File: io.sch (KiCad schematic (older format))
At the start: 13 parts, among them J5 USB_C_Receptacle_USB2.0, J6 Conn_ARM_JTAG_SWD_10, J7 UART, J8 Conn_02x14_Odd_Even

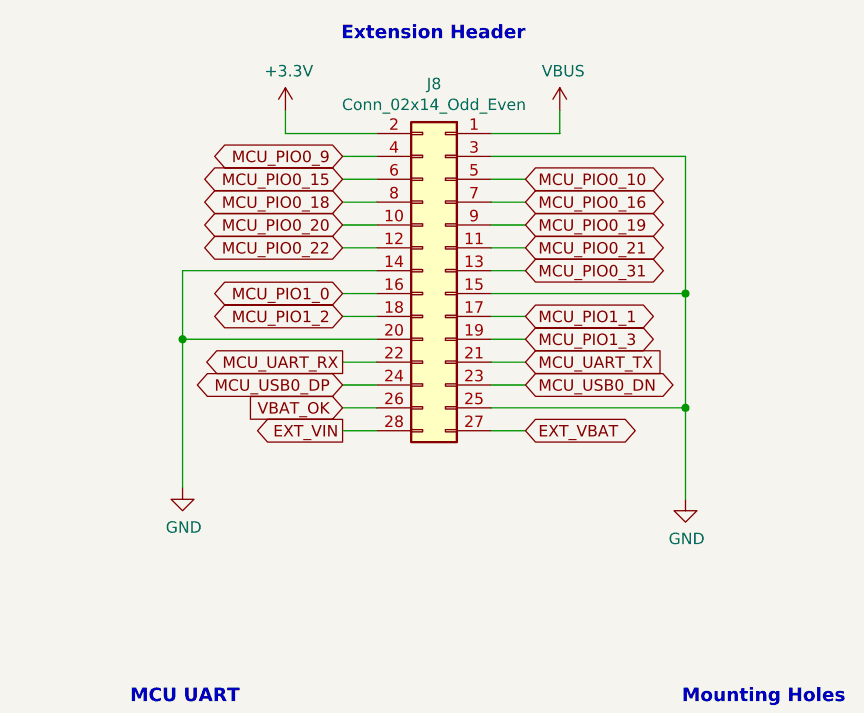
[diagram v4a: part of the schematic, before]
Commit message: Changed pin assignment on mcu and extension header
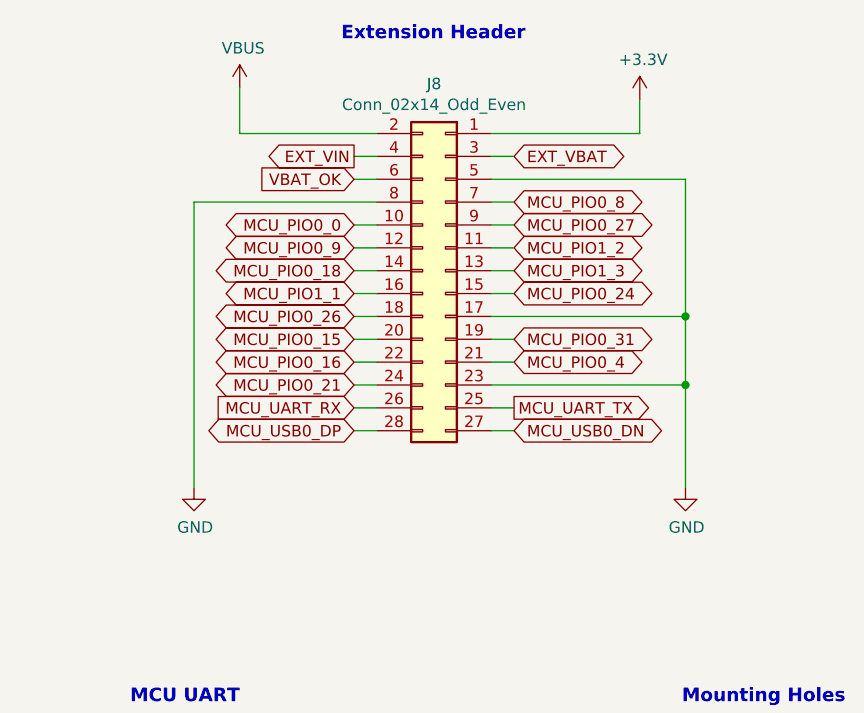
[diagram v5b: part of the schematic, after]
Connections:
- net MCU_PIO0_10 is gone; now on net GND: J8.5 (Pin_5)
- net MCU_PIO0_22 is gone; now on net MCU_PIO0_9: J8.12 (Pin_12)
- net MCU_PIO1_0 is gone; now on net MCU_PIO1_1: J8.16 (Pin_16)
- net +3V3: now also J8.1 (Pin_1); no longer J8.2 (Pin_2)
- net EXT_VBAT: now also J8.3 (Pin_3); no longer J8.27 (Pin_27)
- net EXT_VIN: now also J8.4 (Pin_4); no longer J8.28 (Pin_28)
- net GND: now also J8.17 (Pin_17), J8.23 (Pin_23), J8.8 (Pin_8); no longer J8.14 (Pin_14), J8.15 (Pin_15), J8.20 (Pin_20), J8.25 (Pin_25), J8.3 (Pin_3)
- net MCU_PIO0_15: now also J8.20 (Pin_20); no longer J8.6 (Pin_6)
- net MCU_PIO0_16: now also J8.22 (Pin_22); no longer J8.7 (Pin_7)
- net MCU_PIO0_18: now also J8.14 (Pin_14); no longer J8.8 (Pin_8)
- net MCU_PIO0_21: now also J8.24 (Pin_24); no longer J8.11 (Pin_11)
- net MCU_PIO0_31: now also J8.19 (Pin_19); no longer J8.13 (Pin_13)
- net MCU_PIO0_9: no longer J8.4 (Pin_4)
- net MCU_PIO1_1: no longer J8.17 (Pin_17)
- net MCU_PIO1_2: now also J8.11 (Pin_11); no longer J8.18 (Pin_18)
- net MCU_PIO1_3: now also J8.13 (Pin_13); no longer J8.19 (Pin_19)
- net MCU_UART_RX: now also J8.26 (Pin_26); no longer J8.22 (Pin_22)
- net MCU_UART_TX: now also J8.25 (Pin_25); no longer J8.21 (Pin_21)
- net MCU_USB0_DN: now also J8.27 (Pin_27); no longer J8.23 (Pin_23)
- net MCU_USB0_DP: now also J8.28 (Pin_28); no longer J8.24 (Pin_24)
- net VBAT_OK: now also J8.6 (Pin_6); no longer J8.26 (Pin_26)
- net VBUS: now also J8.2 (Pin_2); no longer J8.1 (Pin_1)
- net MCU_PIO0_19 renamed MCU_PIO0_27
- net MCU_PIO0_20 renamed MCU_PIO0_0
- new net MCU_PIO0_24: J8.15 (Pin_15)
- new net MCU_PIO0_26: J8.18 (Pin_18)
- new net MCU_PIO0_4: J8.21 (Pin_21)
- new net MCU_PIO0_8: J8.7 (Pin_7)
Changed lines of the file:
@@
 	-1   0    0    -1
 $EndComp
-Text GLabel 7650 1700 0    50   BiDi ~ 0
+Text GLabel 8400 1700 2    50   BiDi ~ 0
+EXT_VBAT
+Text GLabel 7700 1700 0    50   Output ~ 0
+EXT_VIN
+Text GLabel 7700 1800 0    50   Input ~ 0
+VBAT_OK
+$Comp
+L power:VBUS #PWR0110
+U 1 1 5FB21530
+P 7200 1400
+F 0 "#PWR0110" H 7200 1250 50  0001 C CNN
+F 1 "VBUS" H 7215 1573 50  0000 C CNN
+F 2 "" H 7200 1400 50  0001 C CNN
+F 3 "" H 7200 1400 50  0001 C CNN
+	1    7200 1400
+	1    0    0    -1
+$EndComp
+Wire Wire Line
+	7200 1400 7200 1600
+Wire Wire Line
+	7200 1600 7800 1600
+$Comp
+L power:+3.3V #PWR0111
+U 1 1 5FB24107
+P 8950 1450
+F 0 "#PWR0111" H 8950 1300 50  0001 C CNN
+F 1 "+3.3V" H 8965 1623 50  0000 C CNN
+F 2 "" H 8950 1450 50  0001 C CNN
+F 3 "" H 8950 1450 50  0001 C CNN
+	1    8950 1450
+	1    0    0    -1
+$EndComp
+Wire Wire Line
+	8300 1600 8950 1600
+Wire Wire Line
+	8950 1600 8950 1450
+Text GLabel 8400 2900 2    50   BiDi ~ 0
+MCU_USB0_DN
+Text GLabel 7700 2900 0    50   BiDi ~ 0
+MCU_USB0_DP
+Text GLabel 8400 2800 2    50   Output ~ 0
+MCU_UART_TX
+Text GLabel 7700 2800 0    50   Input ~ 0
+MCU_UART_RX
+Text GLabel 8400 2600 2    50   BiDi ~ 0
+MCU_PIO0_4
+Text GLabel 7700 2700 0    50   BiDi ~ 0
+MCU_PIO0_21
+Text GLabel 7700 2600 0    50   BiDi ~ 0
+MCU_PIO0_16
+Text GLabel 7700 2500 0    50   BiDi ~ 0
+MCU_PIO0_15
+Text GLabel 8400 2500 2    50   BiDi ~ 0
+MCU_PIO0_31
+Text GLabel 8400 2300 2    50   BiDi ~ 0
+MCU_PIO0_24
+Text GLabel 8400 2200 2    50   BiDi ~ 0
+MCU_PIO1_3
+Text GLabel 8400 2100 2    50   BiDi ~ 0
+MCU_PIO1_2
+Text GLabel 7700 2400 0    50   BiDi ~ 0
+MCU_PIO0_26
+Text GLabel 7700 2300 0    50   BiDi ~ 0
+MCU_PIO1_1
+Text GLabel 7700 2200 0    50   BiDi ~ 0
+MCU_PIO0_18
+Text GLabel 7700 2100 0    50   BiDi ~ 0
 MCU_PIO0_9
-Text GLabel 8450 1800 2    50   BiDi ~ 0
-MCU_PIO0_10
-Text GLabel 7650 1800 0    50   BiDi ~ 0
-MCU_PIO0_15
-Text GLabel 7650 1900 0    50   BiDi ~ 0
-MCU_PIO0_18
-Text GLabel 7650 2000 0    50   BiDi ~ 0
-MCU_PIO0_20
-Text GLabel 7650 2100 0    50   BiDi ~ 0
-MCU_PIO0_22
-Text GLabel 7650 2300 0    50   BiDi ~ 0
-MCU_PIO1_0
-Text GLabel 7650 2400 0    50   BiDi ~ 0
-MCU_PIO1_2
-Text GLabel 7650 2600 0    50   Output ~ 0
-MCU_UART_RX
-Text GLabel 7650 2700 0    50   BiDi ~ 0
-MCU_USB0_DP
-Text GLabel 7650 2800 0    50   Input ~ 0
-VBAT_OK
-Text GLabel 7650 2900 0    50   Output ~ 0
-EXT_VIN
-Text GLabel 8450 1900 2    50   BiDi ~ 0
-MCU_PIO0_16
-Text GLabel 8450 2000 2    50   BiDi ~ 0
-MCU_PIO0_19
-Text GLabel 8450 2100 2    50   BiDi ~ 0
-MCU_PIO0_21
-Text GLabel 8450 2200 2    50   BiDi ~ 0
-MCU_PIO0_31
-Text GLabel 8450 2400 2    50   BiDi ~ 0
-MCU_PIO1_1
-Text GLabel 8450 2500 2    50   BiDi ~ 0
-MCU_PIO1_3
-Text GLabel 8450 2600 2    50   Input ~ 0
-MCU_UART_TX
-Text GLabel 8450 2700 2    50   BiDi ~ 0
-MCU_USB0_DN
-Text GLabel 8450 2900 2    50   BiDi ~ 0
-EXT_VBAT
+Text GLabel 7700 2000 0    50   BiDi ~ 0
+MCU_PIO0_0
+Text GLabel 8400 1900 2    50   BiDi ~ 0
+MCU_PIO0_8
+Text GLabel 8400 2000 2    50   BiDi ~ 0
+MCU_PIO0_27
 $Comp
 L power:GND #PWR0108
-U 1 1 5FB15973
-P 6950 3150
-F 0 "#PWR0108" H 6950 2900 50  0001 C CNN
-F 1 "GND" H 6955 2977 50  0000 C CNN
-F 2 "" H 6950 3150 50  0001 C CNN
-F 3 "" H 6950 3150 50  0001 C CNN
-	1    6950 3150
+U 1 1 5FCCD42F
+P 9150 3150
+F 0 "#PWR0108" H 9150 2900 50  0001 C CNN
+F 1 "GND" H 9155 2977 50  0000 C CNN
+F 2 "" H 9150 3150 50  0001 C CNN
+F 3 "" H 9150 3150 50  0001 C CNN
+	1    9150 3150
 	1    0    0    -1
 $EndComp
 $Comp
 L power:GND #PWR0109
-U 1 1 5FB15D4A
-P 9150 3200
-F 0 "#PWR0109" H 9150 2950 50  0001 C CNN
-F 1 "GND" H 9155 3027 50  0000 C CNN
-F 2 "" H 9150 3200 50  0001 C CNN
-F 3 "" H 9150 3200 50  0001 C CNN
-	1    9150 3200
+U 1 1 5FCCD82E
+P 7000 3150
+F 0 "#PWR0109" H 7000 2900 50  0001 C CNN
+F 1 "GND" H 7005 2977 50  0000 C CNN
+F 2 "" H 7000 3150 50  0001 C CNN
+F 3 "" H 7000 3150 50  0001 C CNN
+	1    7000 3150
 	1    0    0    -1
 $EndComp
 Wire Wire Line
-	8300 1700 9150 1700
+	7000 3150 7000 1900
 Wire Wire Line
-	9150 1700 9150 2300
+	7000 1900 7800 1900
 Wire Wire Line
-	7800 2200 6950 2200
+	8300 1800 9150 1800
 Wire Wire Line
-	6950 2200 6950 2500
+	9150 1800 9150 2400
 Wire Wire Line
-	7800 2500 6950 2500
-Connection ~ 6950 2500
+	8300 2400 9150 2400
+Connection ~ 9150 2400
 Wire Wire Line
-	6950 2500 6950 3150
+	9150 2400 9150 2700
 Wire Wire Line
-	8300 2300 9150 2300
-Connection ~ 9150 2300
+	8300 2700 9150 2700
+Connection ~ 9150 2700
 Wire Wire Line
-	9150 2300 9150 2800
+	9150 2700 9150 3150
 Wire Wire Line
-	8300 2800 9150 2800
-Connection ~ 9150 2800
+	7700 1700 7800 1700
 Wire Wire Line
-	9150 2800 9150 3200
-$Comp
-L power:VBUS #PWR0110
-U 1 1 5FB21530
-P 8600 1500
-F 0 "#PWR0110" H 8600 1350 50  0001 C CNN
-F 1 "VBUS" H 8615 1673 50  0000 C CNN
-F 2 "" H 8600 1500 50  0001 C CNN
-F 3 "" H 8600 1500 50  0001 C CNN
-	1    8600 1500
-	1    0    0    -1
-$EndComp
+	7800 1800 7700 1800
 Wire Wire Line
-	8300 1600 8600 1600
+	7700 2000 7800 2000
 Wire Wire Line
-	8600 1600 8600 1500
-$Comp
-L power:+3.3V #PWR0111
-U 1 1 5FB24107
-P 7400 1500
-F 0 "#PWR0111" H 7400 1350 50  0001 C CNN
-F 1 "+3.3V" H 7415 1673 50  0000 C CNN
-F 2 "" H 7400 1500 50  0001 C CNN
-F 3 "" H 7400 1500 50  0001 C CNN
-	1    7400 1500
-	1    0    0    -1
-$EndComp
+	7800 2100 7700 2100
 Wire Wire Line
-	7400 1500 7400 1600
+	7700 2200 7800 2200
 Wire Wire Line
-	7400 1600 7800 1600
+	7800 2300 7700 2300
 Wire Wire Line
-	7650 1700 7800 1700
+	7700 2400 7800 2400
 Wire Wire Line
-	7800 1800 7650 1800
+	7800 2500 7700 2500
 Wire Wire Line
-	7650 1900 7800 1900
+	7700 2600 7800 2600
 Wire Wire Line
-	7800 2000 7650 2000
+	7800 2700 7700 2700
 Wire Wire Line
-	7650 2100 7800 2100
+	7700 2800 7800 2800
 Wire Wire Line
-	7800 2300 7650 2300
+	7800 2900 7700 2900
 Wire Wire Line
-	7650 2400 7800 2400
+	8300 2900 8400 2900
 Wire Wire Line
-	7800 2600 7650 2600
+	8400 2800 8300 2800
 Wire Wire Line
-	7650 2700 7800 2700
+	8300 2600 8400 2600
 Wire Wire Line
-	7800 2800 7650 2800
+	8400 2500 8300 2500
 Wire Wire Line
-	7650 2900 7800 2900
+	8300 2300 8400 2300
 Wire Wire Line
-	8300 2900 8450 2900
+	8400 2200 8300 2200
 Wire Wire Line
-	8300 2700 8450 2700
+	8300 2100 8400 2100
 Wire Wire Line
-	8300 2600 8450 2600
+	8400 2000 8300 2000
 Wire Wire Line
-	8450 2500 8300 2500
+	8300 1900 8400 1900
 Wire Wire Line
-	8300 2400 8450 2400
-Wire Wire Line
-	8450 2200 8300 2200
-Wire Wire Line
-	8300 2100 8450 2100
-Wire Wire Line
-	8450 2000 8300 2000
-Wire Wire Line
-	8300 1900 8450 1900
-Wire Wire Line
-	8450 1800 8300 1800
+	8300 1700 8400 1700
 $EndSCHEMATC

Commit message: Added footprint assignment
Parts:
- J8: footprint (none) -> Connector_PinHeader_2.54mm:PinHeader_2x14_P2.54mm_Vertical
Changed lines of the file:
@@
 F 0 "J8" H 8150 3017 50  0000 C CNN
 F 1 "Conn_02x14_Odd_Even" H 8150 2926 50  0000 C CNN
-F 2 "" H 8100 2200 50  0001 C CNN
+F 2 "Connector_PinHeader_2.54mm:PinHeader_2x14_P2.54mm_Vertical" H 8100 2200 50  0001 C CNN
 F 3 "~" H 8100 2200 50  0001 C CNN
 	1    8100 2200
